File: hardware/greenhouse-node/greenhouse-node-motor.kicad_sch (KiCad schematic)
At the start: 20 parts, among them J7 Conn_01x02_Male, Q2 2N2222A, Q4 IRF9530N, Q5 IRF530N, Q6 FDP7030DL, Q7 IRF9530N, Q8 IRF530N, U4 L7810

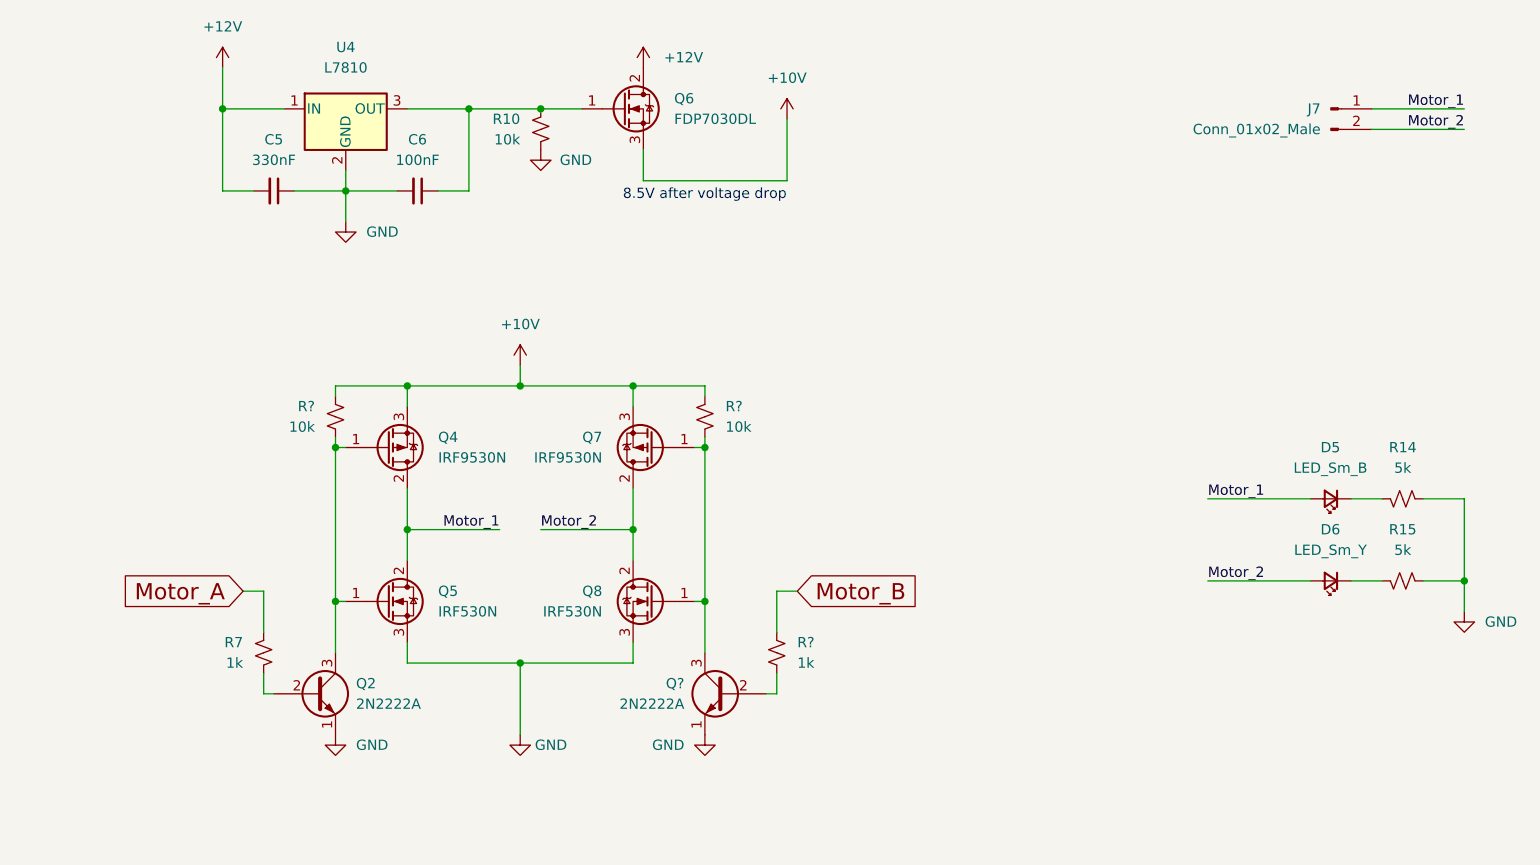
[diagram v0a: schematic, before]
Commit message: Fixed missing traces
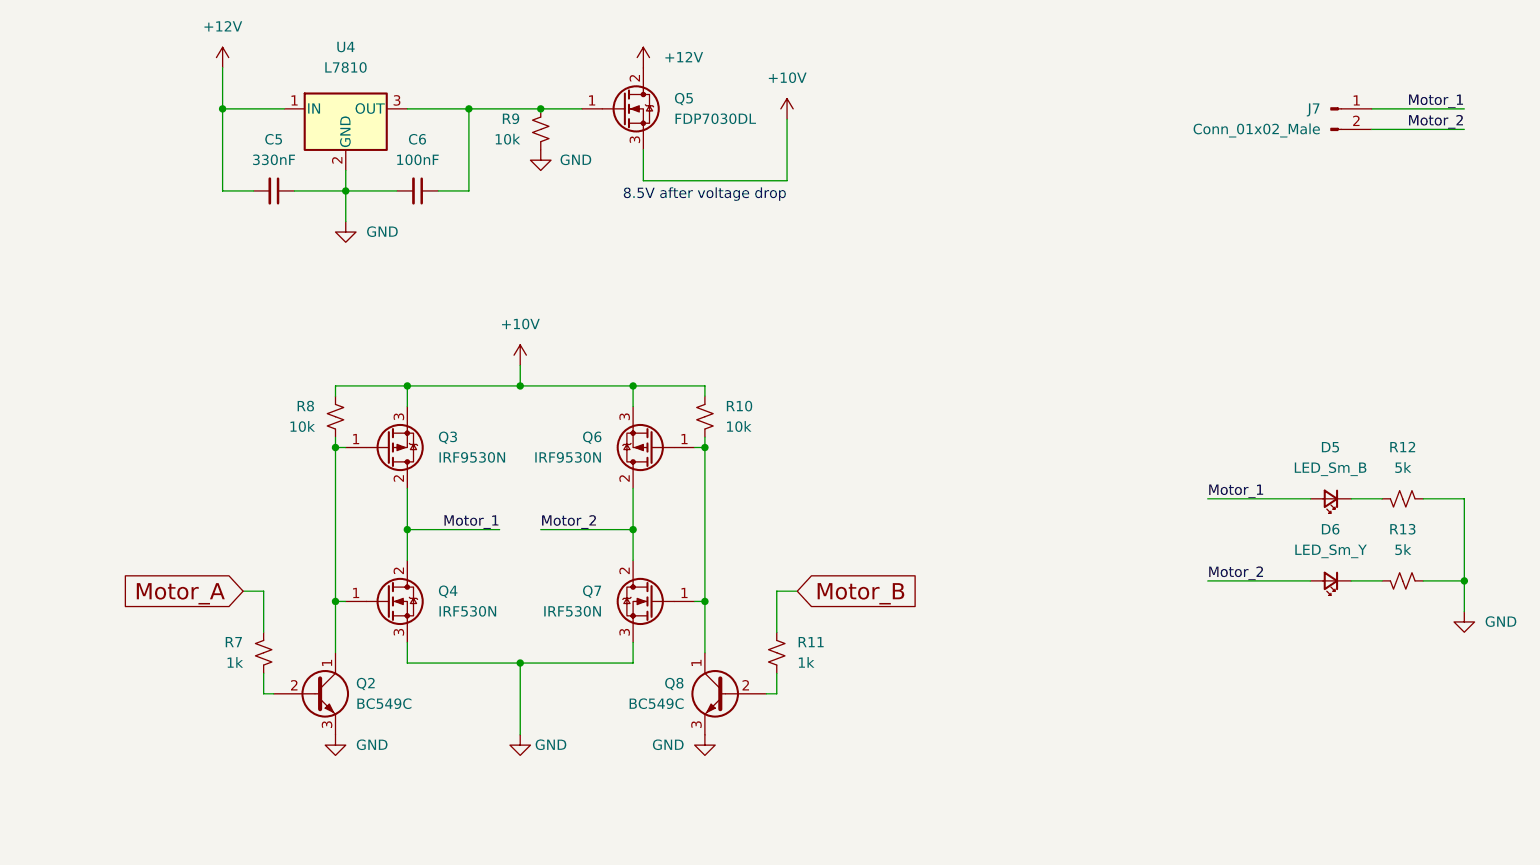
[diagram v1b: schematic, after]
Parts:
- Q2: value 2N2222A -> BC549C; symbol Nick:2N2222A -> Transistor_BJT:BC549
- Q8: renamed from Q?; value 2N2222A -> BC549C; symbol Nick:2N2222A -> Transistor_BJT:BC549
- gave numbers to parts that had none: 3
- renumbered Q4 to Q3, Q5 to Q4, Q6 to Q5, Q7 to Q6, Q8 to Q7, R14 to R12, R15 to R13, R10 to R9
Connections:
- net GND: now also Q2.3 (E), Q8.3 (E); no longer Q2.1 (E), Q8.1 (E)
- net at Q6.1 (G), Q7.1 (G), R10.1: now also Q8.1 (C); no longer Q8.3 (C)
- net at Q3.1 (G), Q4.1 (G), R8.1: now also Q2.1 (C); no longer Q2.3 (C)
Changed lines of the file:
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@@
   (symbol (lib_id "power:+12V") (at 127 53.34 0) (unit 1)
     (in_bom yes) (on_board yes) (fields_autoplaced)
-    (property "Reference" "#PWR027" (id 0) (at 127 57.15 0)
+    (property "Reference" "#PWR026" (id 0) (at 127 57.15 0)
       (effects (font (size 1.27 1.27)) hide)
     )
@@
     (pin "1")
   )
-  (symbol (lib_id "Nick:2N2222A") (at 137.16 130.81 0) (mirror y) (unit 1)
-    (in_bom yes) (on_board yes) (fields_autoplaced)
-    (property "Reference" "Q?" (id 0) (at 132.08 129.5399 0)
-      (effects (font (size 1.27 1.27)) (justify left))
-    )
-    (property "Value" "2N2222A" (id 1) (at 132.08 132.0799 0)
+  (symbol (lib_id "Transistor_BJT:BC549") (at 137.16 130.81 0) (mirror y) (unit 1)
+    (in_bom yes) (on_board yes) (fields_autoplaced)
+    (property "Reference" "Q8" (id 0) (at 132.08 129.5399 0)
+      (effects (font (size 1.27 1.27)) (justify left))
+    )
+    (property "Value" "BC549C" (id 1) (at 132.08 132.0799 0)
       (effects (font (size 1.27 1.27)) (justify left))
     )
@@
       (effects (font (size 1.27 1.27) italic) (justify left) hide)
     )
-    (property "Datasheet" "https://www.onsemi.com/pub/Collateral/2N3903-D.PDF" (id 3) (at 137.16 130.81 0)
+    (property "Datasheet" "https://www.onsemi.com/pub/Collateral/BC550-D.pdf" (id 3) (at 137.16 130.81 0)
       (effects (font (size 1.27 1.27)) (justify left) hide)
     )
@@
   (symbol (lib_id "power:GND") (at 228.6 120.65 0) (unit 1)
     (in_bom yes) (on_board yes) (fields_autoplaced)
-    (property "Reference" "#PWR031" (id 0) (at 228.6 127 0)
+    (property "Reference" "#PWR029" (id 0) (at 228.6 127 0)
       (effects (font (size 1.27 1.27)) hide)
     )
@@
   (symbol (lib_id "Transistor_FET:IRF9540N") (at 95.25 100.33 0) (mirror x) (unit 1)
     (in_bom yes) (on_board yes) (fields_autoplaced)
-    (property "Reference" "Q4" (id 0) (at 101.6 99.0599 0)
+    (property "Reference" "Q3" (id 0) (at 101.6 99.0599 0)
       (effects (font (size 1.27 1.27)) (justify left))
     )
@@
   (symbol (lib_id "power:GND") (at 90.17 72.39 0) (unit 1)
     (in_bom yes) (on_board yes) (fields_autoplaced)
-    (property "Reference" "#PWR023" (id 0) (at 90.17 78.74 0)
+    (property "Reference" "#PWR022" (id 0) (at 90.17 78.74 0)
       (effects (font (size 1.27 1.27)) hide)
     )
@@
   (symbol (lib_id "power:+12V") (at 74.93 53.34 0) (unit 1)
     (in_bom yes) (on_board yes) (fields_autoplaced)
-    (property "Reference" "#PWR021" (id 0) (at 74.93 57.15 0)
+    (property "Reference" "#PWR020" (id 0) (at 74.93 57.15 0)
       (effects (font (size 1.27 1.27)) hide)
     )
@@
   (symbol (lib_id "power:+10V") (at 111.76 90.17 0) (unit 1)
     (in_bom yes) (on_board yes) (fields_autoplaced)
-    (property "Reference" "#PWR024" (id 0) (at 111.76 93.98 0)
+    (property "Reference" "#PWR023" (id 0) (at 111.76 93.98 0)
       (effects (font (size 1.27 1.27)) hide)
     )
@@
   (symbol (lib_id "Transistor_FET:IRF540N") (at 124.46 58.42 0) (unit 1)
     (in_bom yes) (on_board yes) (fields_autoplaced)
-    (property "Reference" "Q6" (id 0) (at 130.81 57.1499 0)
+    (property "Reference" "Q5" (id 0) (at 130.81 57.1499 0)
       (effects (font (size 1.27 1.27)) (justify left))
     )
@@
   (symbol (lib_id "Transistor_FET:IRF9540N") (at 128.27 100.33 180) (unit 1)
     (in_bom yes) (on_board yes) (fields_autoplaced)
-    (property "Reference" "Q7" (id 0) (at 121.92 99.0599 0)
+    (property "Reference" "Q6" (id 0) (at 121.92 99.0599 0)
       (effects (font (size 1.27 1.27)) (justify left))
     )
@@
     (pin "3")
   )
-  (symbol (lib_id "Nick:2N2222A") (at 86.36 130.81 0) (unit 1)
+  (symbol (lib_id "Transistor_BJT:BC549") (at 86.36 130.81 0) (unit 1)
     (in_bom yes) (on_board yes) (fields_autoplaced)
     (property "Reference" "Q2" (id 0) (at 91.44 129.5399 0)
       (effects (font (size 1.27 1.27)) (justify left))
     )
-    (property "Value" "2N2222A" (id 1) (at 91.44 132.0799 0)
+    (property "Value" "BC549C" (id 1) (at 91.44 132.0799 0)
       (effects (font (size 1.27 1.27)) (justify left))
     )
@@
       (effects (font (size 1.27 1.27) italic) (justify left) hide)
     )
-    (property "Datasheet" "https://www.onsemi.com/pub/Collateral/2N3903-D.PDF" (id 3) (at 86.36 130.81 0)
+    (property "Datasheet" "https://www.onsemi.com/pub/Collateral/BC550-D.pdf" (id 3) (at 86.36 130.81 0)
       (effects (font (size 1.27 1.27)) (justify left) hide)
     )
@@
   (symbol (lib_id "Transistor_FET:IRF540N") (at 95.25 119.38 0) (unit 1)
     (in_bom yes) (on_board yes) (fields_autoplaced)
-    (property "Reference" "Q5" (id 0) (at 101.6 118.1099 0)
+    (property "Reference" "Q4" (id 0) (at 101.6 118.1099 0)
       (effects (font (size 1.27 1.27)) (justify left))
     )
@@
   (symbol (lib_id "power:+10V") (at 144.78 59.69 0) (unit 1)
     (in_bom yes) (on_board yes) (fields_autoplaced)
-    (property "Reference" "#PWR029" (id 0) (at 144.78 63.5 0)
+    (property "Reference" "#PWR028" (id 0) (at 144.78 63.5 0)
       (effects (font (size 1.27 1.27)) hide)
     )
@@
   (symbol (lib_id "Device:R_Small_US") (at 143.51 125.73 180) (unit 1)
     (in_bom yes) (on_board yes) (fields_autoplaced)
-    (property "Reference" "R?" (id 0) (at 146.05 124.4599 0)
+    (property "Reference" "R11" (id 0) (at 146.05 124.4599 0)
       (effects (font (size 1.27 1.27)) (justify right))
     )
@@
   (symbol (lib_id "Device:R_Small_US") (at 88.9 96.52 180) (unit 1)
     (in_bom yes) (on_board yes) (fields_autoplaced)
-    (property "Reference" "R?" (id 0) (at 86.36 95.2499 0)
+    (property "Reference" "R8" (id 0) (at 86.36 95.2499 0)
       (effects (font (size 1.27 1.27)) (justify left))
     )
@@
   (symbol (lib_id "Device:R_Small_US") (at 134.62 96.52 0) (mirror x) (unit 1)
     (in_bom yes) (on_board yes) (fields_autoplaced)
-    (property "Reference" "R?" (id 0) (at 137.16 95.2499 0)
+    (property "Reference" "R10" (id 0) (at 137.16 95.2499 0)
       (effects (font (size 1.27 1.27)) (justify left))
     )
@@
   (symbol (lib_id "Device:R_Small_US") (at 114.3 60.96 0) (mirror x) (unit 1)
     (in_bom yes) (on_board yes) (fields_autoplaced)
-    (property "Reference" "R10" (id 0) (at 111.76 59.6899 0)
+    (property "Reference" "R9" (id 0) (at 111.76 59.6899 0)
       (effects (font (size 1.27 1.27)) (justify right))
     )
@@
   (symbol (lib_id "Device:R_Small_US") (at 220.98 116.84 270) (mirror x) (unit 1)
     (in_bom yes) (on_board yes) (fields_autoplaced)
-    (property "Reference" "R15" (id 0) (at 220.98 110.49 90))
+    (property "Reference" "R13" (id 0) (at 220.98 110.49 90))
     (property "Value" "5k" (id 1) (at 220.98 113.03 90))
     (property "Footprint" "Resistor_THT:R_Axial_DIN0204_L3.6mm_D1.6mm_P7.62mm_Horizontal" (id 2) (at 220.98 116.84 0)
@@
   (symbol (lib_id "Device:R_Small_US") (at 220.98 106.68 270) (mirror x) (unit 1)
     (in_bom yes) (on_board yes) (fields_autoplaced)
-    (property "Reference" "R14" (id 0) (at 220.98 100.33 90))
+    (property "Reference" "R12" (id 0) (at 220.98 100.33 90))
     (property "Value" "5k" (id 1) (at 220.98 102.87 90))
     (property "Footprint" "Resistor_THT:R_Axial_DIN0204_L3.6mm_D1.6mm_P7.62mm_Horizontal" (id 2) (at 220.98 106.68 0)
@@
   (symbol (lib_id "Transistor_FET:IRF540N") (at 128.27 119.38 0) (mirror y) (unit 1)
     (in_bom yes) (on_board yes) (fields_autoplaced)
-    (property "Reference" "Q8" (id 0) (at 121.92 118.1099 0)
+    (property "Reference" "Q7" (id 0) (at 121.92 118.1099 0)
       (effects (font (size 1.27 1.27)) (justify left))
     )
@@
   (symbol (lib_id "power:GND") (at 114.3 63.5 0) (mirror y) (unit 1)
     (in_bom yes) (on_board yes)
-    (property "Reference" "#PWR026" (id 0) (at 114.3 69.85 0)
+    (property "Reference" "#PWR025" (id 0) (at 114.3 69.85 0)
       (effects (font (size 1.27 1.27)) hide)
     )
@@
   (symbol (lib_id "power:GND") (at 111.76 135.89 0) (unit 1)
     (in_bom yes) (on_board yes)
-    (property "Reference" "#PWR025" (id 0) (at 111.76 142.24 0)
+    (property "Reference" "#PWR024" (id 0) (at 111.76 142.24 0)
       (effects (font (size 1.27 1.27)) hide)
     )
@@
   (symbol (lib_id "power:GND") (at 88.9 135.89 0) (unit 1)
     (in_bom yes) (on_board yes) (fields_autoplaced)
-    (property "Reference" "#PWR020" (id 0) (at 88.9 142.24 0)
+    (property "Reference" "#PWR021" (id 0) (at 88.9 142.24 0)
       (effects (font (size 1.27 1.27)) hide)
     )
@@
   (symbol (lib_id "power:GND") (at 134.62 135.89 0) (mirror y) (unit 1)
     (in_bom yes) (on_board yes) (fields_autoplaced)
-    (property "Reference" "#PWR?" (id 0) (at 134.62 142.24 0)
-      (effects (font (size 1.27 1.27)) hide)
-    )
+    (property "Reference" "#PWR027" (id 0) (at 134.62 142.24 0)
+      (effects (font (size 1.27 1.27)) hide)
+    )

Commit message: Change LEDs to use H-bridge circuit
Previously using GND
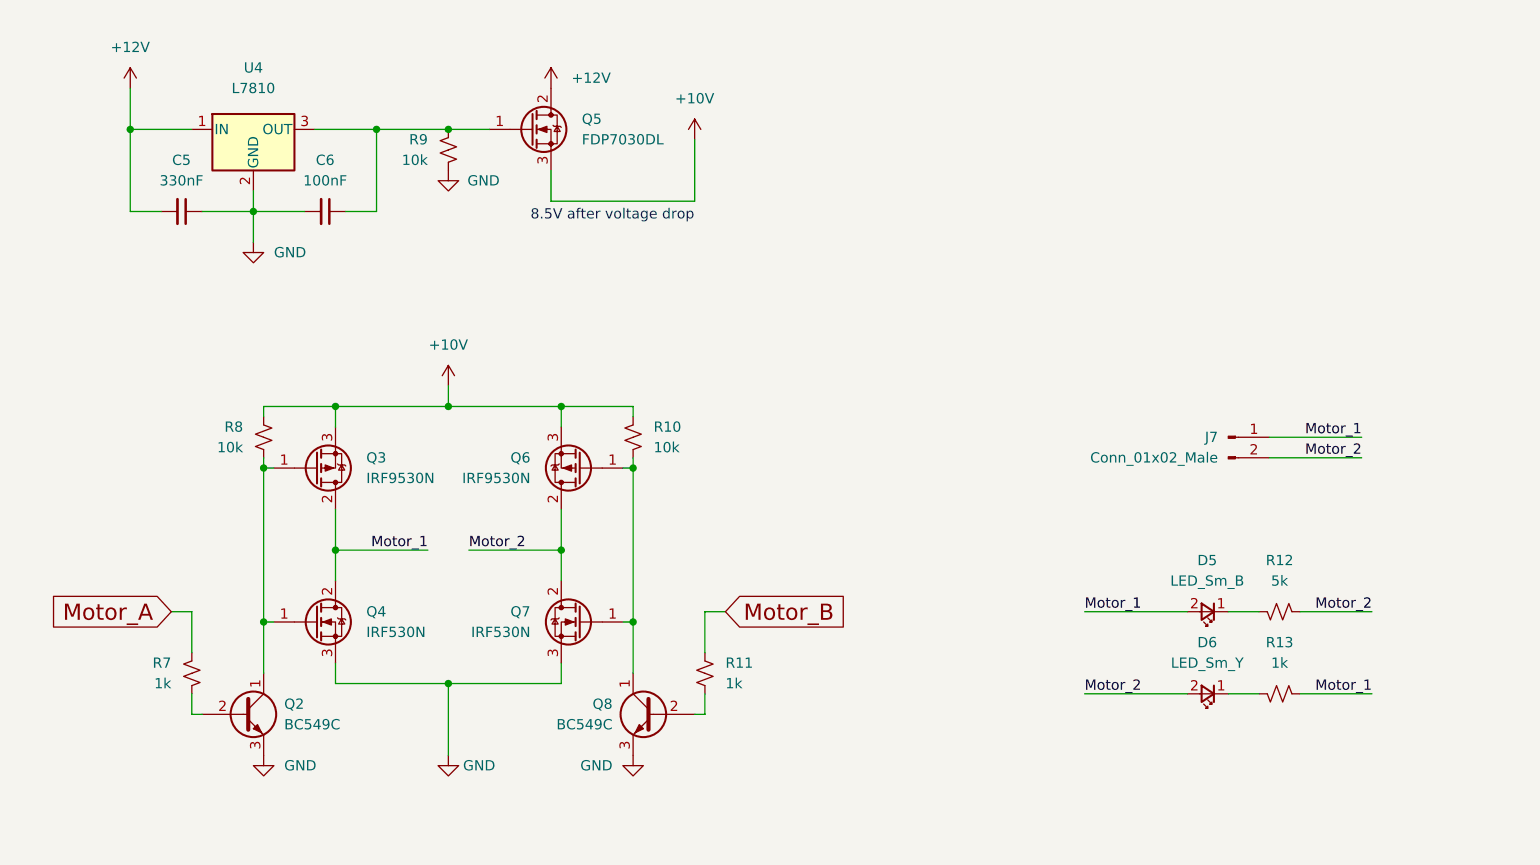
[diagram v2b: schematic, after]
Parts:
- R13: value 5k -> 1k
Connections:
- net GND: no longer R12.1, R13.1
- net Motor_1: now also R13.1
- net Motor_2: now also R12.1
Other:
- moved on the sheet: C5, C6, J7, Q2, Q3, Q4, Q5, Q6, Q7, Q8, R10, R11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

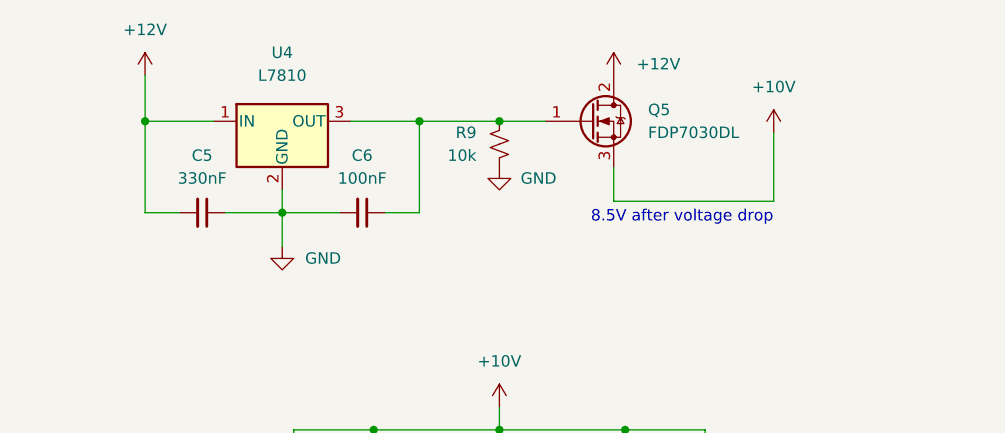
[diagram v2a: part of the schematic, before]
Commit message: Remove voltage regulator
Provide +10V with buck converter instead; perhaps regulate actuator with PWM to control speed
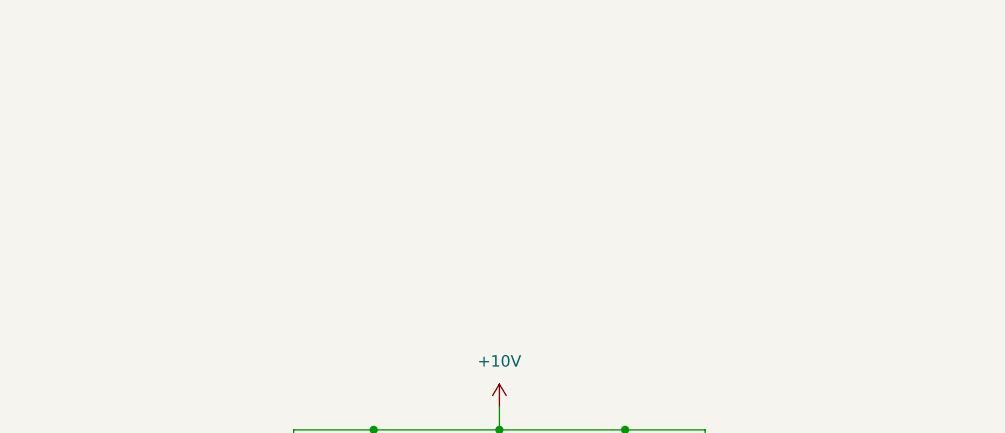
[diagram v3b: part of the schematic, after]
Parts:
- removed C5: 330nF, Capacitor_THT:C_Disc_D4.7mm_W2.5mm_P5.00mm, symbol Device:C_Small
- removed C6: 100nF, Capacitor_THT:C_Disc_D4.7mm_W2.5mm_P5.00mm, symbol Device:C_Small
- removed Q5: FDP7030DL, Package_TO_SOT_THT:TO-220-3_Horizontal_TabDown, symbol Transistor_FET:IRF540N
- removed R9: 10k, Resistor_THT:R_Axial_DIN0204_L3.6mm_D1.6mm_P7.62mm_Horizontal, symbol Device:R_Small_US
- removed U4: L7810, Nick:TO-92L_Inline_Regulator, symbol Regulator_Linear:L7809
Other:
- note removed: "8.5V after voltage drop"

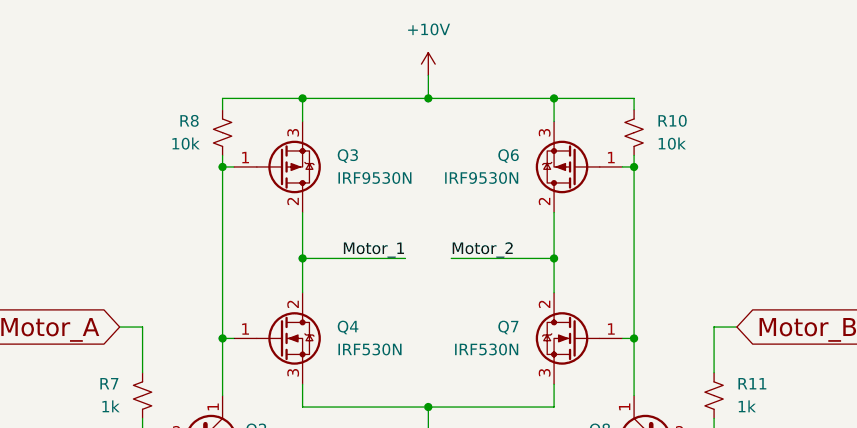
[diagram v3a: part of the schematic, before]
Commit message: Change pull-ups to 2k
Required for PWM (which we may not implement), so may not be totally necessary
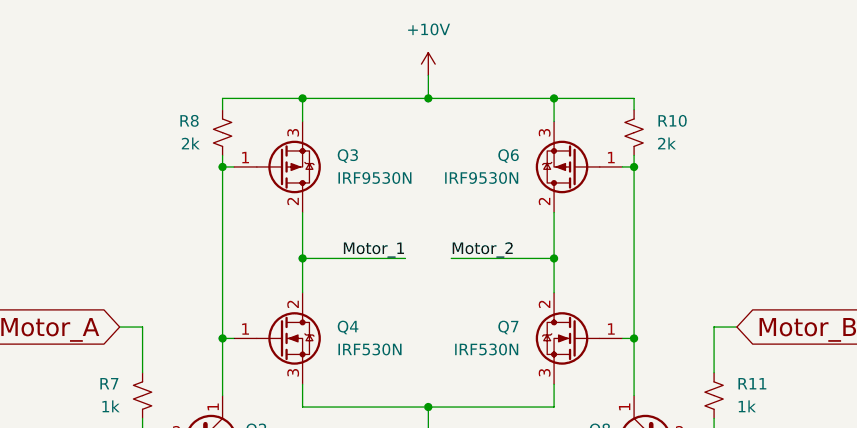
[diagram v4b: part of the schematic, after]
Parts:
- R10, R8: value 10k -> 2k
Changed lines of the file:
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@@
       (effects (font (size 1.27 1.27)) (justify left))
     )
-    (property "Value" "10k" (id 1) (at 77.47 100.3299 0)
+    (property "Value" "2k" (id 1) (at 77.47 100.3299 0)
       (effects (font (size 1.27 1.27)) (justify left))
     )
@@
       (effects (font (size 1.27 1.27)) (justify left))
     )
-    (property "Value" "10k" (id 1) (at 128.27 100.3299 0)
+    (property "Value" "2k" (id 1) (at 128.27 100.3299 0)
       (effects (font (size 1.27 1.27)) (justify left))
     )
